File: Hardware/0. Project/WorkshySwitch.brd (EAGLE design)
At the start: 32 x 40 mm, 25 parts, among them CN1 ICSP, IC1 LM1117-3.3, K1 G3MB-202P, Q1 BC848, U1 ATMEGA328P-AU, U2 HLK-PM01

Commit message: PCB layout under dev
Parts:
- CN1: device con-molex:7395-06 -> pinhead:1X06
- moved X3 92.3 mm to (27.5, 38.0), turned to 180 degrees
- moved CN1 74.4 mm to (23.0, 51.5), turned to 180 degrees
- moved PCB1 41.5 mm to (19.9, 11.7)
- moved X1 40.2 mm to (5.50, 38.0), turned to 180 degrees
- moved X2 39.8 mm to (16.5, 38.0), turned to 180 degrees
- moved U1 38.0 mm to (-1.56, 53.8)
- moved R5 26.2 mm to (2.50, 30.0), turned to 0 degrees
- moved U2 1.58 mm to (19.4, 17.5)
- moved F1 1.00 mm to (7.50, 15.0)
- moved F2 0.50 mm to (7.00, 29.5), turned to 180 degrees
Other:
- board size 32 x 40 mm -> 30 x 45 mm

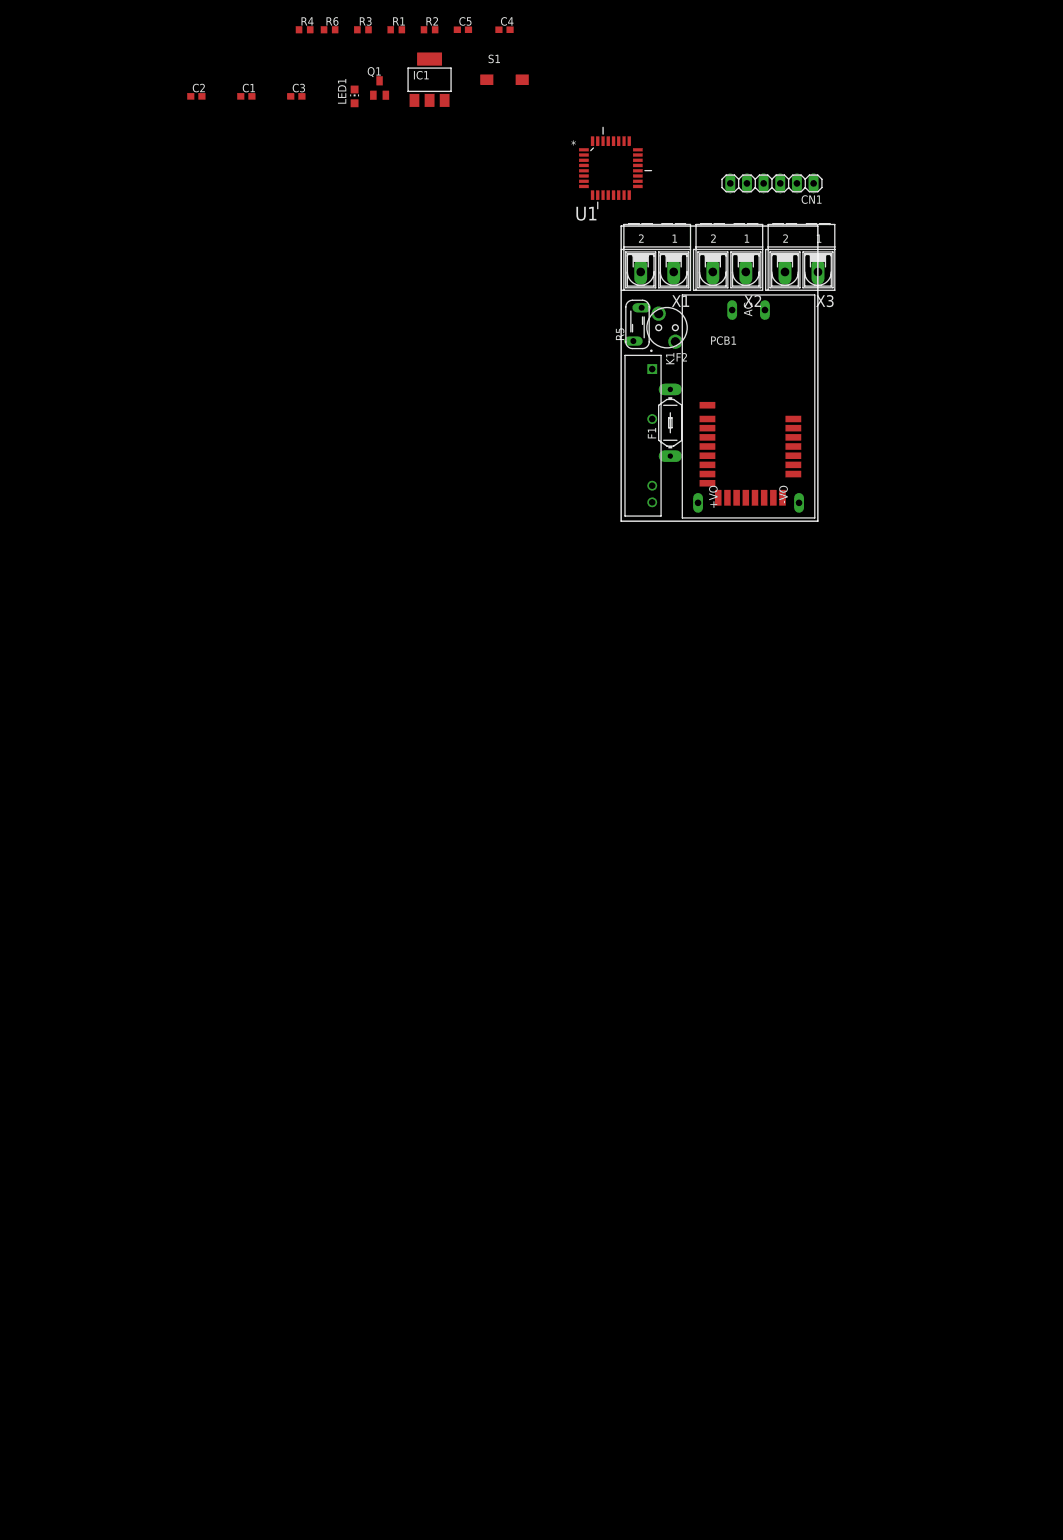
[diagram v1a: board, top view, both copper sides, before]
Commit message: New hardware design approch
- The previous approach would be too large.
- Now, MCU and BLE module don't exists anymore.
- A new MCU with embedded BLE was added: CC2541.
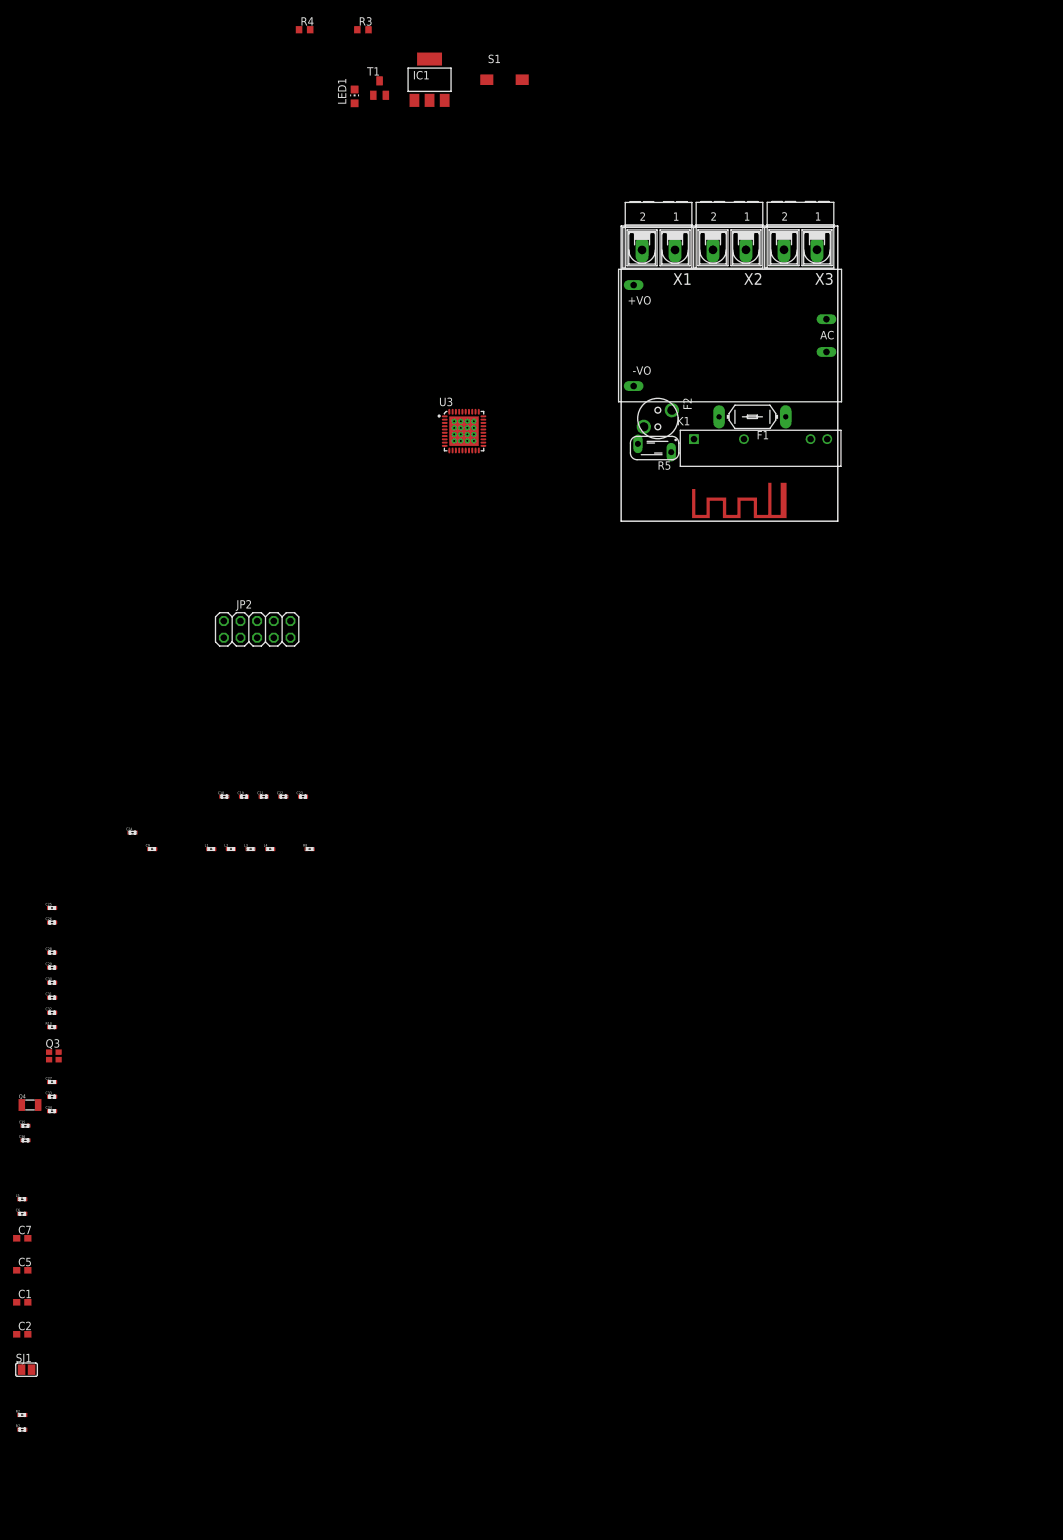
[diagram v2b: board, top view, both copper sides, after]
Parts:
- removed C3: 100 nF, rcl:C0603
- removed C4: 10 uF, rcl:C0603
- removed CN1: ICSP, pinhead:1X06
- removed PCB1: BLE-1010, BLE-1010:BLE-1010
- removed R1, R6: 10k, rcl:R0603
- removed U1: ATMEGA328P-AU, Atmel_By_element14_Batch_1-00:QFP80P900X900X120-32N
- added A3: 50R, PCB Antenna:MIFA
- added C18, C19: 18pF, smd-ipc:C0402
- added C21, C22, C24: 1pF, smd-ipc:C0402
- added C23: DNM, smd-ipc:C0402
- added C25: 220pF, smd-ipc:C0402
- added C26, C28, C29, C30, C31: 100nF, smd-ipc:C0402
- added C27, C32: 1uF, smd-ipc:C0402
- added C33, C34: 12pF, smd-ipc:C0402
- added C35, C36: 15pF, smd-ipc:C0402
- added C6: 2.2uF, smd-ipc:C0402
- added C7: 100nF, rcl:C0603
- added C9: 100n, smd-ipc:C0402
- added JP2: (no value), pinhead:2X05
- added L1, L2: 2nH, smd-ipc:C0402
- added L3: 1nH, smd-ipc:C0402
- added L4: 3nH, smd-ipc:C0402
- added L5: BLM15HG102SN1D, smd-ipc:C0402
- added Q3: 32-MHz, crystal:FA-128
- added Q4: 32.768-kHz, crystal-geyer_V1_0:3.2X1.5
- added R10: 56k, smd-ipc:C0402
- added R7: 10k, smd-ipc:C0402
- added R8: 2.7k, smd-ipc:C0402
- added SJ1: (no value), jumper:SJ
- added U3: CC2541, CC2541F256RHAT:QFN50P600X600X100-41N
- C2: value 100nF -> 10uF
- C5: value 10 uF -> 10uF
- R2: device rcl:R0603 -> smd-ipc:C0402
- S1: value DTSM-3 -> (none)
- moved R2 220.2 mm to (-91.3, -136.3)
- moved C5 200.7 mm to (-91.3, -114.2)
- moved C2 190.6 mm to (-91.3, -124.0)
- moved C1 187.0 mm to (-91.3, -119.1)
- moved R5 19.0 mm to (5.10, 11.2), turned to 90 degrees
- moved K1 18.0 mm to (21.3, 11.1), turned to 0 degrees
- moved F2 13.9 mm to (5.60, 15.7), turned to 270 degrees
- moved F1 12.6 mm to (20.0, 15.9), turned to 180 degrees
- moved U2 11.2 mm to (16.6, 28.3), turned to 180 degrees
- moved X3 3.38 mm to (27.4, 41.4)
- moved X2 3.37 mm to (16.5, 41.4)
- moved X1 3.37 mm to (5.71, 41.4)
- renumbered Q1 to T1
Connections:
- removed net BLE_RX: PCB1.6, U1.31
- removed net BLE_TX: PCB1.5, U1.30
- removed net BLE_WAKE: PCB1.24, R2.2, U1.1
- removed net ICSP_MISO: CN1.1, U1.10
- removed net ICSP_MOSI: CN1.4, U1.9
- removed net ICSP_RESET: CN1.5, R1.1, U1.29
- removed net ICSP_SCK: CN1.3, U1.11
- new net +4.1V: C25.1, C26.1, C28.1, C29.1, C30.1, C31.1, C32.1, C6.1, JP2.2, L5.1, R2.2, R7.2, SJ1.2, U3.10, U3.21, U3.24, U3.27, U3.28, U3.29, U3.31, U3.39
- new net DEBUG_CLK: JP2.3, U3.34
- new net DEBUG_DATA: JP2.4, U3.35
- new net DEBUG_RESET: JP2.7, R8.1
- new net MCU_RESET: C9.1, R8.2, U3.20
- new net N$10: JP2.9, SJ1.1
- new net N$12: C19.1, C22.2, L1.1
- new net N$13: C22.1, C23.2, L2.2, L3.1
- new net N$14: C19.2, U3.26
- new net N$15: C18.2, C21.1, L2.1
- new net N$44: C24.1, L3.2, L4.1
- new net N$45: A3.FEED, L4.2
- new net N$46: C27.1, U3.40
- new net N$47: R10.2, U3.30
- new net N$48: C33.1, Q3.1, U3.23
- new net N$49: C34.1, Q3.3, U3.22
- new net N$50: C35.1, Q4.1, U3.32
- new net N$51: C36.1, Q4.2, U3.33
- net 3.3V: now also C1.1, C2.1, L5.2; no longer C2.2, C3.1, C4.1, CN1.2, PCB1.17, PCB1.22, R1.2, R2.1, R6.1, U1.18, U1.4, U1.6
- net 5V: now also C7.1
- net BUTTON_PROG: now also R2.1, U3.8; no longer U1.24
- net GND: now also A3.GND, C1.2, C2.2, C21.2, C23.1, C24.2, C25.2, C26.2, C27.2, C28.2, C29.2, C30.2, C31.2, C32.2, C33.2, C34.2, C35.2, C36.2, C6.2, C7.2, C9.2, JP2.1, L1.2, Q3.2, Q3.4, R10.1, U3.1, U3.2, U3.3, U3.4, U3.41, U3.42, U3.43, U3.44, U3.45, U3.46, U3.47, U3.48, U3.49, U3.50, U3.51, U3.52, U3.53, U3.54, U3.55, U3.56, U3.57; no longer C1.1, C2.1, C3.2, C4.2, CN1.6, PCB1.1, PCB1.21, PCB1.23, U1.21, U1.3, U1.5
- net LED_STATUS: now also U3.11; no longer U1.25
- net LOAD_CONTROL: now also U3.9; no longer U1.23
- net N$11: now also C18.1, U3.25; no longer C1.2, U1.20
- net PHY_SWITCH_STATUS: now also R7.1, U3.7; no longer R6.2, U1.32
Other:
- board size 30 x 45 mm -> 33 x 45 mm

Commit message: Reduced number of PTR connectors
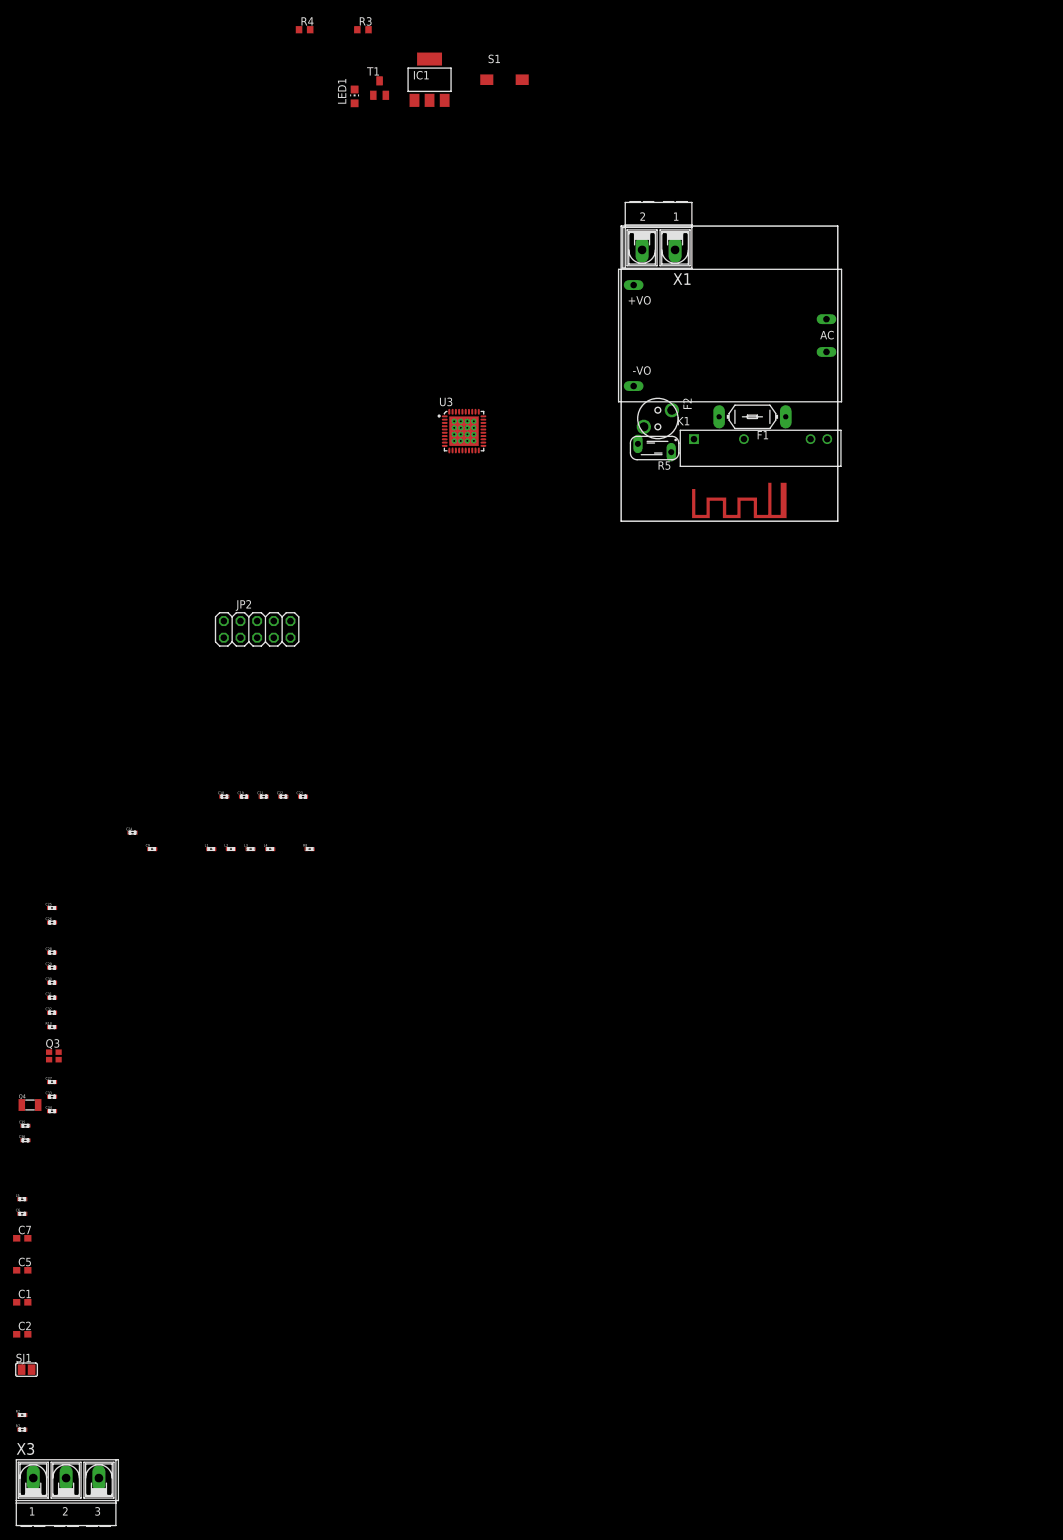
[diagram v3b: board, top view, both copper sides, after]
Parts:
- removed X2: (no value), con-ptr500:AK500/2-H
- X3: device con-ptr500:AK500/2-H -> con-ptr500:AK500/3-H
- moved X3 218.2 mm to (-84.6, -145.9), turned to 0 degrees
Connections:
- removed net N$2: F2.2, X3.1
- removed net N$7: K1.1, X2.1
- new net L1_PHASE: F2.2, K1.1, X3.1
- net N$8: now also X3.3; no longer X2.2
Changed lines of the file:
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@@
 <attribute name="PRICE" value="None" x="-30.38" y="39.73" size="1.778" layer="27" rot="R180" display="off"/>
-</element>
-<element name="X3" library="con-ptr500" library_urn="urn:adsk.eagle:library:181" package="AK500/2-H" package3d_urn="urn:adsk.eagle:package:9901/1" value="" x="27.35" y="41.38" smashed="yes" rot="R180">
-<attribute name="MF" value="" x="-37.42" y="76.94" size="1.778" layer="27" rot="R180" display="off"/>
-<attribute name="MPN" value="" x="-37.42" y="76.94" size="1.778" layer="27" rot="R180" display="off"/>
-<attribute name="NAME" x="32.43" y="37.824" size="1.778" layer="25" ratio="10" rot="R180"/>
-<attribute name="OC_FARNELL" value="unknown" x="-37.42" y="76.94" size="1.778" layer="27" rot="R180" display="off"/>
-<attribute name="OC_NEWARK" value="unknown" x="-37.42" y="76.94" size="1.778" layer="27" rot="R180" display="off"/>
-<attribute name="VALUE" x="32.43" y="50.905" size="1.778" layer="27" ratio="10" rot="R180"/>
-</element>
-<element name="X2" library="con-ptr500" library_urn="urn:adsk.eagle:library:181" package="AK500/2-H" package3d_urn="urn:adsk.eagle:package:9901/1" value="" x="16.52" y="41.37" smashed="yes" rot="R180">
-<attribute name="MF" value="" x="-2.53" y="97.25" size="1.778" layer="27" rot="R180" display="off"/>
-<attribute name="MPN" value="" x="-2.53" y="97.25" size="1.778" layer="27" rot="R180" display="off"/>
-<attribute name="NAME" x="21.6" y="37.814" size="1.778" layer="25" ratio="10" rot="R180"/>
-<attribute name="OC_FARNELL" value="unknown" x="-2.53" y="97.25" size="1.778" layer="27" rot="R180" display="off"/>
-<attribute name="OC_NEWARK" value="unknown" x="-2.53" y="97.25" size="1.778" layer="27" rot="R180" display="off"/>
-<attribute name="VALUE" x="21.6" y="50.895" size="1.778" layer="27" ratio="10" rot="R180"/>
 </element>
 <element name="X1" library="con-ptr500" library_urn="urn:adsk.eagle:library:181" package="AK500/2-H" package3d_urn="urn:adsk.eagle:package:9901/1" value="" x="5.71" y="41.36" smashed="yes" rot="R180">
@@
 <attribute name="NAME" x="-92.315" y="-138.155" size="0.4" layer="25"/>
 <attribute name="VALUE" x="-92.315" y="-139.285" size="0.4" layer="27"/>
+</element>
+<element name="X3" library="con-ptr500" library_urn="urn:adsk.eagle:library:181" package="AK500/3-H" package3d_urn="urn:adsk.eagle:package:9899/1" value="" x="-84.63" y="-145.91" smashed="yes">
+<attribute name="MF" value="" x="-84.63" y="-145.91" size="1.778" layer="27" display="off"/>
+<attribute name="MPN" value="" x="-84.63" y="-145.91" size="1.778" layer="27" display="off"/>
+<attribute name="NAME" x="-92.2246" y="-142.354" size="1.778" layer="25" ratio="10"/>
+<attribute name="OC_FARNELL" value="unknown" x="-84.63" y="-145.91" size="1.778" layer="27" display="off"/>
+<attribute name="OC_NEWARK" value="unknown" x="-84.63" y="-145.91" size="1.778" layer="27" display="off"/>
+<attribute name="VALUE" x="-92.2246" y="-155.435" size="1.778" layer="27" ratio="10"/>
 </element>
 </elements>
@@
 <wire x1="-15.08" y1="67.31" x2="-26.9" y2="12.48" width="0" layer="19" extent="1-1"/>
 </signal>
-<signal name="N$2">
+<signal name="L1_PHASE">
+<contactref element="F2" pad="2"/>
 <contactref element="X3" pad="1"/>
-<contactref element="F2" pad="2"/>
-<wire x1="3.4613" y1="14.38" x2="29.8646" y2="41.38" width="0" layer="19" extent="1-1"/>
+<contactref element="K1" pad="1"/>
+<wire x1="3.4613" y1="14.38" x2="-89.6338" y2="-145.91" width="0" layer="19" extent="1-1"/>
+<wire x1="11.11" y1="12.51" x2="3.4613" y2="14.38" width="0" layer="19" extent="1-1"/>
 </signal>
 <signal name="N$3">
-<contactref element="X3" pad="2"/>
 <contactref element="U2" pad="P$2"/>
 <contactref element="R5" pad="2"/>
-<wire x1="31.31" y1="30.8" x2="24.8354" y2="41.38" width="0" layer="19" extent="1-1"/>
-<wire x1="2.56" y1="11.785" x2="31.31" y2="30.8" width="0" layer="19" extent="1-1"/>
+<contactref element="X3" pad="2"/>
+<wire x1="2.56" y1="11.785" x2="-84.63" y2="-145.91" width="0" layer="19" extent="1-1"/>
+<wire x1="31.31" y1="30.8" x2="2.56" y2="11.785" width="0" layer="19" extent="1-1"/>
 </signal>
 <signal name="3.3V">
@@
 <wire x1="-47.41" y1="74.93" x2="-37.78" y2="64.94" width="0" layer="19" extent="1-1"/>
 </signal>
-<signal name="N$7">
-<contactref element="X2" pad="1"/>
-<contactref element="K1" pad="1"/>
-<wire x1="11.11" y1="12.51" x2="19.0346" y2="41.37" width="0" layer="19" extent="1-1"/>
-</signal>
 <signal name="N$8">
-<contactref element="X2" pad="2"/>
 <contactref element="K1" pad="2"/>
-<wire x1="18.73" y1="12.51" x2="14.0054" y2="41.37" width="0" layer="19" extent="1-1"/>
+<contactref element="X3" pad="3"/>
+<wire x1="18.73" y1="12.51" x2="-79.6262" y2="-145.91" width="0" layer="19" extent="1-1"/>
 </signal>
 <signal name="PHY_SWITCH_STATUS">

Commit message: PCB layout under dev
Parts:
- removed F1: SF70E, Thermal Fuse:LITTLEFUSE
- removed IC1: LM1117-3.3, v-reg:SOT223
- added F3: SF70E, fuse:LITTLEFUSE
- added U1: LM1117-3.3, REG1117:SOT223
- X1: device con-ptr500:AK500/2-H -> con-ptr500:AK500/2
- X3: device con-ptr500:AK500/3-H -> con-ptr500:AK500/3
- moved X3 208.8 mm to (8.06, 41.2), turned to 180 degrees
- moved C2 207.0 mm to (54.4, 23.1), flipped to the bottom, turned to 270 degrees
- moved C1 201.9 mm to (52.1, 23.1), flipped to the bottom, turned to 270 degrees
- moved C5 196.0 mm to (48.7, 22.9), flipped to the bottom, turned to 90 degrees
- moved C7 190.6 mm to (45.9, 22.9), flipped to the bottom, turned to 90 degrees
- moved R2 189.6 mm to (52.2, -12.3), flipped to the bottom, turned to 90 degrees
- moved R7 189.4 mm to (50.0, -12.3), flipped to the bottom, turned to 90 degrees
- moved L5 178.2 mm to (65.1, -18.1), flipped to the bottom, turned to 90 degrees
- moved C6 177.3 mm to (62.9, -18.1), flipped to the bottom, turned to 90 degrees
- moved SJ1 161.7 mm to (2.00, 3.15), turned to 270 degrees
- moved C34 154.0 mm to (28.3, 12.3), flipped to the bottom, turned to 270 degrees
- moved C36 153.6 mm to (15.4, 16.6), flipped to the bottom, turned to 180 degrees
- moved C35 153.4 mm to (17.3, 16.6), flipped to the bottom
- moved C33 150.0 mm to (26.7, 10.3), flipped to the bottom, turned to 180 degrees
- moved Q4 148.9 mm to (16.3, 15.1), flipped to the bottom
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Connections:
- net 3.3V: now also U1.2, U1.4; no longer IC1.4
- net 5V: now also U1.3; no longer IC1.3
- net GND: now also U1.1; no longer IC1.1
- net N$4: now also F3.2; no longer F1.1
- net N$9: now also F3.1; no longer F1.2
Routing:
- net DEBUG_DATA: track 0.00 -> 23.7 mm
- net DEBUG_CLK: track 0.00 -> 19.4 mm
- net +4.1V: track 0.00 -> 13.6 mm
- net N$51: track 0.00 -> 7.86 mm
- net N$48: track 0.00 -> 5.06 mm
- net N$49: track 0.00 -> 4.59 mm
- net N$50: track 0.00 -> 4.57 mm
- net N$13: track 0.00 -> 4.29 mm
- net MCU_RESET: track 0.00 -> 2.31 mm
- net N$44: track 0.00 -> 2.31 mm
- net N$47: track 0.00 -> 1.93 mm
- net N$15: track 0.00 -> 1.84 mm
- net N$12: track 0.00 -> 1.81 mm
- net N$46: track 0.00 -> 1.48 mm
- net N$45: track 0.00 -> 1.48 mm
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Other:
- board size 33 x 45 mm -> 35 x 45 mm
